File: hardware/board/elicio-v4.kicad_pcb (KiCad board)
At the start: 2 copper layers, 30.1 x 55.2 mm, 61 parts, among them J2 202656-0021, J3 HDR-3-RA, J4 TC2030-NL, P1 SIG1, P2 SIG2, P3 REF, P4 CHARGE_VBUS, P5 CHARGE_GND, Q1 WPM3027-3, Q2 NMOS, Q3 NMOS, Q4 NMOS, SW1 1TS015A, U1 ISP1807-LR, U2 ADS1292IRSMT, U3 BQ25100YFPR, U4 TLV71330PDQNT, U5 TPS7A0230PDQNR

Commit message: wip(board v4): placement reliefs, GND pours, own router and finisher; not routed
The committed elicio-v4.kicad_pcb is placed with locked pre-routes and two
unfilled GND pour outlines. It carries no free routing and is NOT routed.

- build_v4.py: placement reliefs around U1/U2/U4 (R7, R27, C9/C10, R12,
  R15, C14, R16/R17, divider pocket), GND pours on F and B, net names on
  numberless mask/paste aperture pads.
- v4_route_pf.py: negotiated-congestion grid router (Freerouting 2.4.1 left
  18 connections open on the earlier W18 placement).
- v4_route_fix.py: DRC-driven finisher with local rip-up.
- scripts/board/route_v4.py: Freerouting DSN/route/SES wrapper.
- tests/test_board_v4.py: Contact-safety and fold checks.
- docs/fab/board-v4-design.md: design note; §9 and §10 not final.

Scratch routing state: the last negotiated pass converged with 0 conflicts
and has not yet been DRC-checked, finished or pour-filled.

Co-Authored-By: Claude Opus 5.5 <noreply@anthropic.com>
Claude-Session: https://claude.ai/code/session_01RSpwhJjxHd7GLkEqrgCckN
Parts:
- moved R17 3.20 mm to (14.6, 28.6), turned to -90 degrees
- moved C9 1.10 mm to (10.2, 18.5)
- moved C10 1.10 mm to (9.10, 18.6)
- moved R18 0.35 mm to (11.8, 25.6)
- moved R19 0.35 mm to (13.3, 26.5), turned to 0 degrees
- moved R20 0.35 mm to (11.8, 26.4)
- moved R21 0.35 mm to (11.8, 27.2)
- moved Q2 0.35 mm to (13.3, 27.6)
- moved R16 0.20 mm to (14.6, 27.1), turned to -90 degrees
- moved R7 0.09 mm to (11.1, 25.5)
- turned R12 to 180 degrees
- turned R15 to 0 degrees
- turned R27 to -90 degrees
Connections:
- U4 pad : (no net) -> AFE_VIN
- U5 pad : (no net) -> VBAT
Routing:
- added copper zone on B.Cu, net GND
- added copper zone on F.Cu, net GND

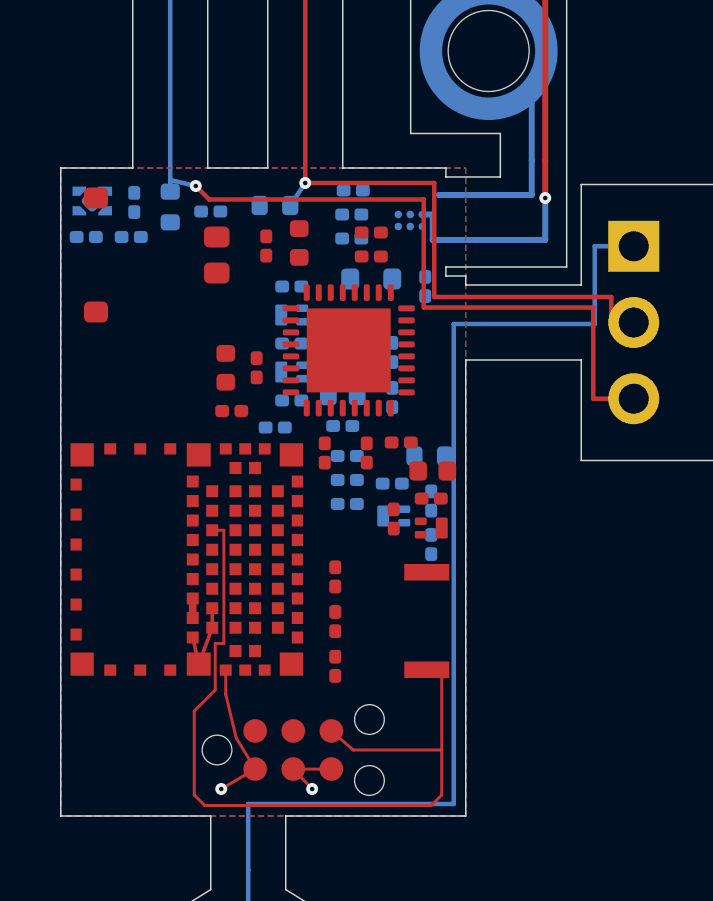
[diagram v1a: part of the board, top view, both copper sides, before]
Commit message: board(v4): every net but GND routed, GND pours filled; NOT routed
elicio-v4.kicad_pcb: all nets except GND are routed (961 segments, 45 vias
with the locked pre-routes) by v4_route_pf.py; both GND pours are filled.
kicad-cli DRC: 0 shorts, 0 clearance errors, 13 starved_thermal errors
(GND pads) and 36 unconnected items, all GND (37 GND pieces). release.py
--routed was not run and would refuse. Do not order.

- build_v4.py: C14 turned so its VBAT pad faces east; with it facing west
  VBAT walled off AFE_VIN on B (the last two-net conflict).
- board-v4-design.md: §9 routing status (router results, placement reliefs,
  every open GND join with pads and mm, next steps, rebuild commands);
  §10.1 flat table; §10.2 folded table still owed.
- v4_tables.py: docstring no longer claims a folded table.

Co-Authored-By: Claude Opus 5.5 <noreply@anthropic.com>
Claude-Session: https://claude.ai/code/session_01RSpwhJjxHd7GLkEqrgCckN
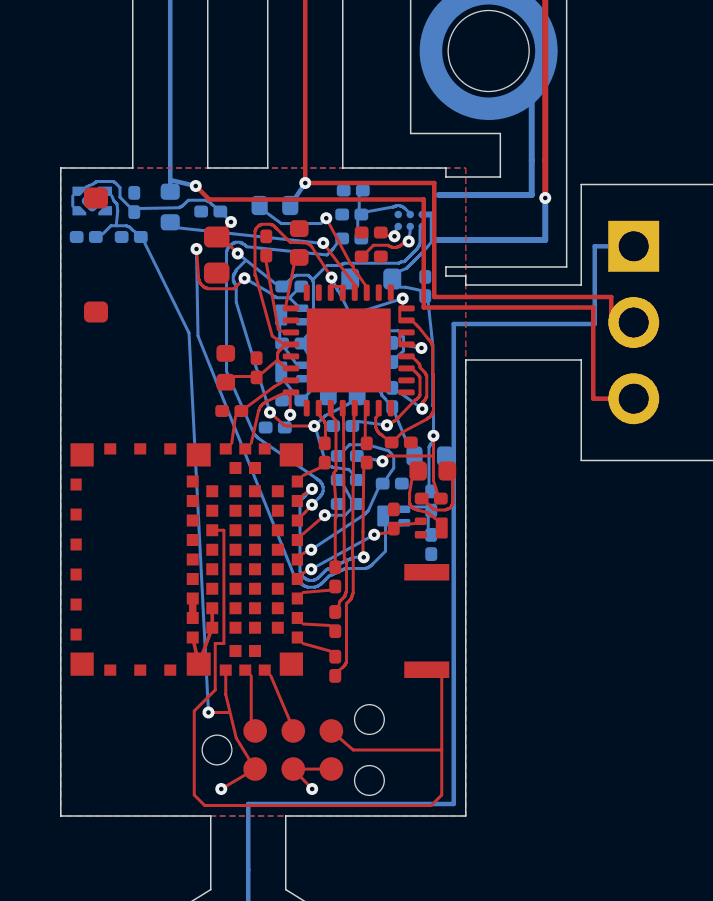
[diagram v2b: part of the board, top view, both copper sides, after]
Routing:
- net VBAT: track 0.00 -> 27.0 mm, vias 0 -> 4
- net AFE_EN_HW: track 0.00 -> 21.3 mm, vias 0 -> 2
- net +3V0: track 0.00 -> 20.1 mm, vias 0 -> 2
- net +VDD: track 4.83 -> 23.8 mm, vias 1 -> 2
- net CHG_MON: track 0.00 -> 14.5 mm, vias 0 -> 1
- net VBUS: track 18.2 -> 30.8 mm, vias 2 -> 4
- net AFE_DRDY: track 0.00 -> 8.83 mm, vias 0 -> 2
- net AFE_MISO_AFE: track 0.00 -> 8.66 mm
- net AFE_IN1P: track 0.00 -> 6.58 mm, vias 0 -> 1
- net AFE_SCLK_AFE: track 0.00 -> 6.43 mm
- net RLD_FB: track 0.00 -> 6.31 mm, vias 0 -> 1
- net VBUS_DET: track 0.00 -> 6.05 mm, vias 0 -> 1
- net AFE_MOSI_AFE: track 0.00 -> 4.91 mm
- net AFE_IN1N: track 0.00 -> 4.77 mm, vias 0 -> 1
- net RLDINV: track 0.00 -> 4.17 mm, vias 0 -> 1
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
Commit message: board(v4): relief 5, VCAP1 pre-route, solid-pad rule; PCB at 0 DRC errors, 10 open; NOT routed
- build_v4.py: west stack 0.10 west (9.85, R24 9.30), C8/C14/C11 turned so
  their GND pads face east, Q3/R15 turned, VCAP1 locked on F west of U2
  (design note §9.2 relief 5; relief 4 reversed).
- elicio-v4.kicad_dru: U2.33, U4.5, U5.5 and J2.MP connect solid; every
  other GND pad keeps its relief and the starved-thermal check is not
  relaxed (§9.3). No Contact, creepage or clearance rule changed.
- elicio-v4.kicad_pcb: routed by v4_route_pf.py with three regional GND nets,
  finished by v4_finish.sh, saved with filled zones. DRC with the project
  rules: 0 errors, 0 shorts, 0 starved thermals, 10 unconnected items
  (5 GND, 2 AFE_VIN, AFE_DRDY, CHG_MON, VBUS_DET), listed with pads and
  gaps in §9.4. release.py --routed refuses on them; the plain release
  writes review outputs with routed: false.
- scripts/board/release.py: the pads-without-net blocker counts copper pads
  only; KiCad's paste-only pads (blank number) cannot carry a net.
- tests/test_board_v4.py: a property saved by KiCad continues on the next
  line; the value regex no longer demands the closing paren.

Co-Authored-By: Claude Fable 5.1 <noreply@anthropic.com>
Claude-Session: https://claude.ai/code/session_01UK16n13AdpykZ3bHg6Ep1F
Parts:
- added R31: 220k, Resistor_SMD:R_0402_1005Metric, F.Cu at (22.4, 16.8)
- added R32: 220k, Resistor_SMD:R_0402_1005Metric, F.Cu at (18.0, 21.1)
- added R33: 220k, Resistor_SMD:R_0402_1005Metric, F.Cu at (22.4, 27.1)
- moved J3 1.31 mm to (22.4, 19.4)
- moved C5 0.10 mm to (9.85, 23.8)
- moved Q1 0.10 mm to (9.85, 22.8)
- moved Q3 0.10 mm to (9.85, 20.9), turned to 0 degrees
- moved R14 0.10 mm to (9.85, 21.9)
- moved R15 0.10 mm to (9.85, 19.9), turned to 180 degrees
- moved R24 0.10 mm to (9.30, 24.6)
- turned C11 to 0 degrees
- turned C14 to 0 degrees
- turned C8 to 0 degrees
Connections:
- J3 pad 1: REF -> BENCH_SIG1
- J3 pad 2: SIG2 -> BENCH_SIG2
- J3 pad 3: SIG1 -> BENCH_REF
- U1 pad 14: unconnected-(U1-VSS-Pad14) -> GND
- U1 pad 16: unconnected-(U1-VSS-Pad16) -> GND
- U1 pad 18: unconnected-(U1-VSS-Pad18) -> GND
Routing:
- net GND: track 13.0 -> 75.3 mm, vias 1 -> 16
- net AFE_IN1P: track 6.58 -> 29.5 mm, vias 1 -> 4
- net SIG1: track 33.8 -> 11.5 mm, vias 1 -> 0
- net SIG2: track 38.8 -> 23.2 mm
- net REF: track 37.5 -> 24.5 mm
- net RLD_FB: track 6.31 -> 17.4 mm
- net VBAT: track 27.0 -> 36.6 mm, vias 4 -> 5
- net AFE_EN_HW: track 21.3 -> 15.8 mm, vias 2 -> 0
- net AFE_IN1N: track 4.77 -> 9.78 mm
- net BENCH_SIG2: track 0.00 -> 4.22 mm
- net AFE_SCLK_AFE: track 6.43 -> 9.95 mm, vias 0 -> 2
- net AFE_VIN: track 3.54 -> 7.01 mm
- net +3V0: track 20.1 -> 16.7 mm, vias 2 -> 4
- net BENCH_REF: track 0.00 -> 2.73 mm
- net BENCH_SIG1: track 0.00 -> 2.71 mm
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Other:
- board size 30.1 x 55.2 mm -> 31.1 x 55.2 mm

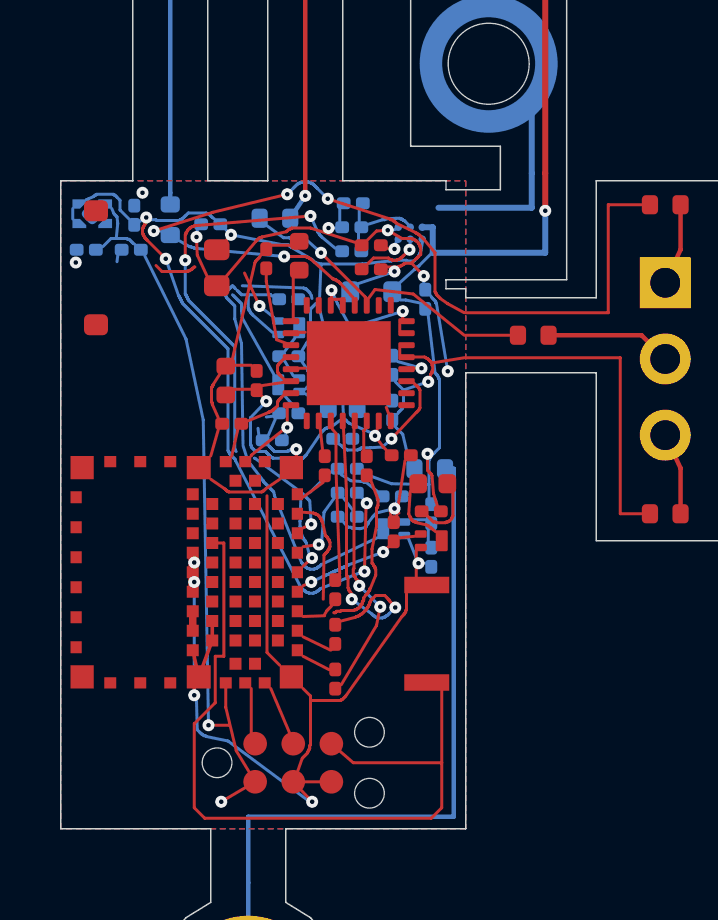
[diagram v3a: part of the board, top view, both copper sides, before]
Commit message: board v4: routed board from pass 6 (t-0019); DRC 0 errors, 0 unconnected after refill; routed release passes
Router run 5 (v4_route_pf.py, GND split A/B/C) converged at round 16 with 0 conflicts;
v4_finish.sh closed GND and cleared 3 starved thermals. DRC with --refill-zones and
--schematic-parity: 0 errors, 0 unconnected, 25 warnings (24 lib_footprint_mismatch, the
documented +VDD via_dangling at (7.60, 36.70)), 2 parity (J2 MP pads, documented).
release.py --board elicio-v4 --routed exits 0 with routed: true. U1 pad nets unchanged.
Design note §9/§10 not yet updated.

Co-Authored-By: Claude Opus 5.5 <noreply@anthropic.com>
Claude-Session: https://claude.ai/code/session_01U4y3Vd9KrCnaj8gNYUDRvj
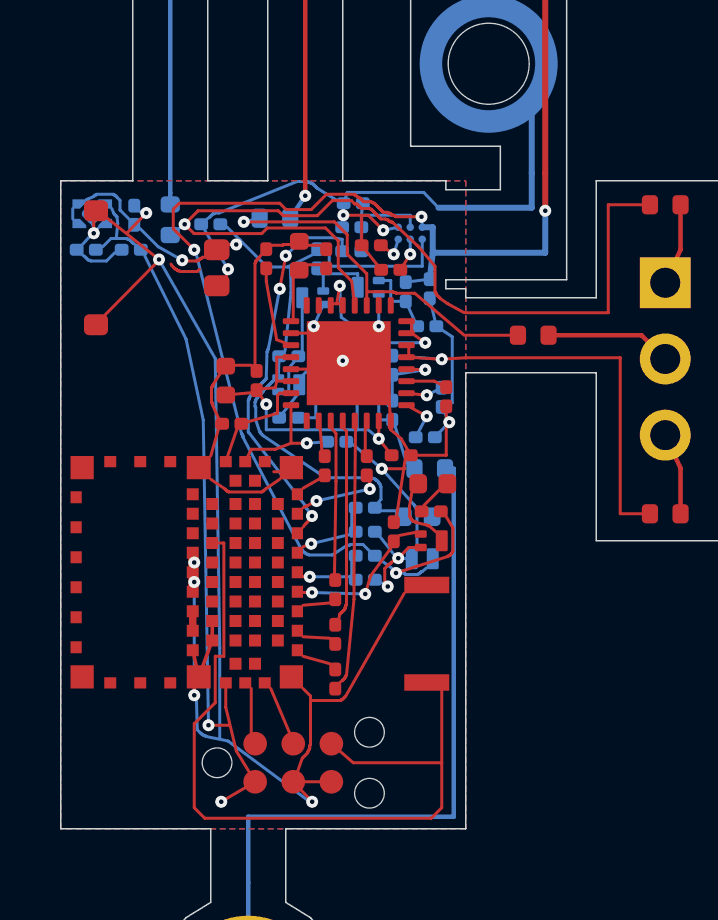
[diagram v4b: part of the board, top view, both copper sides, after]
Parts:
- added C17: 100nF, Capacitor_SMD:C_0201_0603Metric, F.Cu at (11.1, 18.6)
- added R34: 10k, Resistor_SMD:R_0201_0603Metric, B.Cu at (14.9, 23.2)
- added R35: 10k, Resistor_SMD:R_0201_0603Metric, B.Cu at (14.4, 24.6)
- C11: value 100nF -> 1uF; moved to F.Cu
- D1: footprint Diode_SMD:D_SOD-523 -> Diode_SMD:D_SOD-882
- Q2, Q3, Q4: value NMOS -> PMZ290UNE2
- moved D1 9.06 mm to (14.3, 28.6)
- moved Q2 8.09 mm to (12.5, 19.6)
- moved R17 7.70 mm to (14.4, 20.9), turned to 0 degrees
- moved R16 7.45 mm to (13.8, 19.7)
- moved C14 4.38 mm to (14.2, 27.2)
- moved C11 3.72 mm to (15.1, 23.2), turned to -90 degrees
- moved R18 2.96 mm to (12.4, 28.5)
- moved R19 2.92 mm to (12.4, 29.3)
- moved R24 2.15 mm to (11.4, 24.7), turned to 0 degrees
- moved R15 1.65 mm to (10.8, 18.6), turned to -90 degrees
- moved Q3 1.28 mm to (10.7, 19.9), turned to 180 degrees
- moved R20 0.78 mm to (12.4, 26.9)
- moved R21 0.78 mm to (12.4, 27.7), turned to 0 degrees
- moved R13 0.65 mm to (13.2, 19.0), turned to 180 degrees
- moved C3 0.38 mm to (14.6, 19.6), turned to -90 degrees
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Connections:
- U2 pad 25: unconnected-(U2-GPIO2-Pad25) -> AFE_GPIO2
- U2 pad 26: unconnected-(U2-GPIO1-Pad26) -> AFE_GPIO1
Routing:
- net GND: track 75.3 -> 110.0 mm, vias 16 -> 17
- net VBUS: track 30.8 -> 48.9 mm, vias 3 -> 5
- net AFE_EN_HW: track 15.8 -> 2.55 mm
- net VBAT: track 36.6 -> 25.0 mm, vias 5 -> 2
- net AFE_DRDY: track 8.98 -> 2.55 mm, vias 0 -> 2
- net CHG_MON: track 17.1 -> 12.7 mm
- net AFE_VIN: track 7.01 -> 2.67 mm
- net AFE_SCLK_AFE: track 9.95 -> 6.43 mm, vias 2 -> 0
- net VCAP2: track 4.28 -> 1.37 mm, vias 1 -> 0
- net VBUS_DET: track 4.75 -> 1.93 mm
- net +3V0: track 16.7 -> 19.3 mm
- net AFE_IN1N: track 9.78 -> 12.3 mm
- net AFE_GATE: track 1.08 -> 3.47 mm
- net RLD_FB: track 17.4 -> 19.7 mm
- net AFE_START: track 2.44 -> 4.30 mm
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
